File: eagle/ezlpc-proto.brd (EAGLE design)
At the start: 38.1 x 22.9 mm, 61 parts, among them J1 MICRO USB, Q1 12Mhz, T1 MMBT3906, U1 PRTR5V0U2X, U2 MIC5225-3.3v, U3 LPC11U35FHI33/501

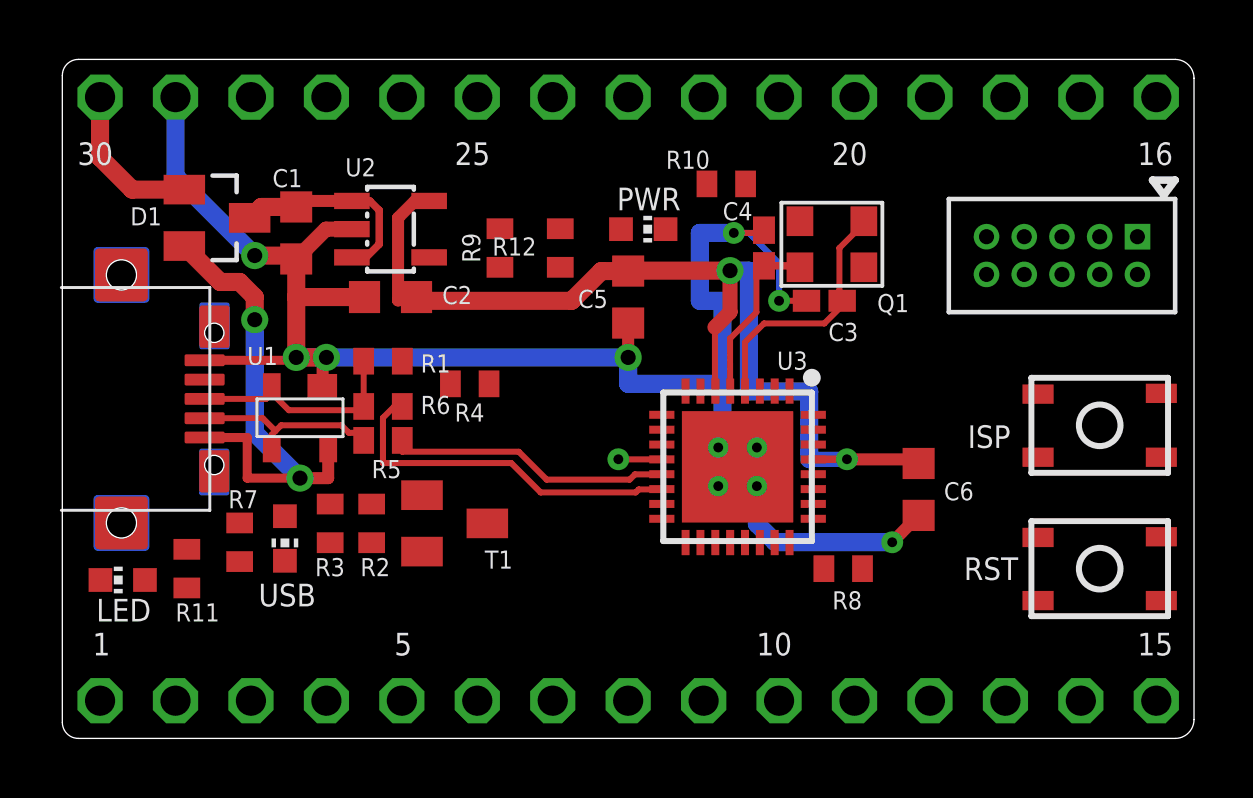
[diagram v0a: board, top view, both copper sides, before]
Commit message: Reduced board height by 0.1" to better fit solderless breadboards.
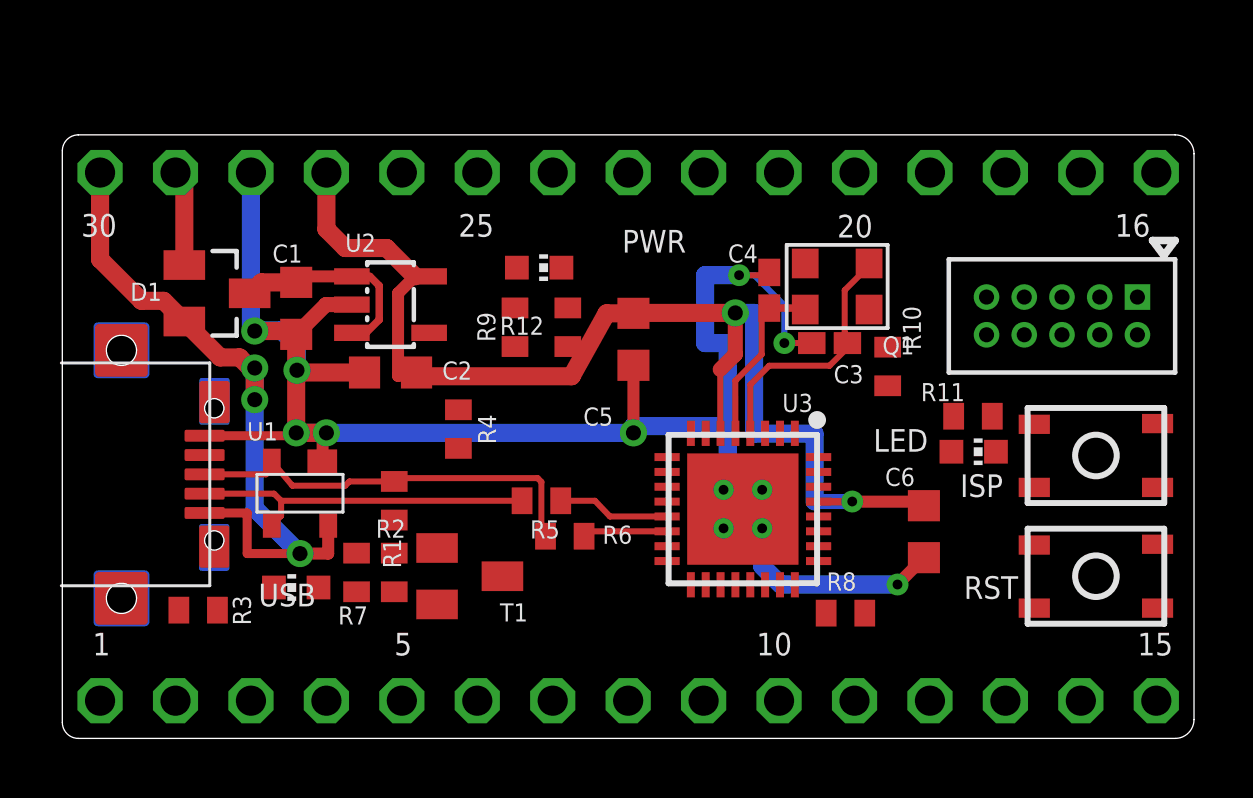
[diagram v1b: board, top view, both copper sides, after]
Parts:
- moved LED2 29.0 mm to (30.7, 9.65), turned to 270 degrees
- moved R11 27.0 mm to (30.7, 10.8), turned to 180 degrees
- moved R10 8.21 mm to (27.8, 12.5), turned to 90 degrees
- moved R6 7.52 mm to (16.9, 6.81)
- moved R5 5.71 mm to (16.1, 8.00)
- moved R3 5.32 mm to (4.57, 4.32), turned to 0 degrees
- moved R1 4.71 mm to (11.2, 8.00), turned to 270 degrees
- moved R7 4.07 mm to (9.91, 5.59), turned to 90 degrees
- moved LED3 3.74 mm to (16.1, 15.8)
- moved R9 2.71 mm to (15.2, 13.8)
- moved R12 2.68 mm to (17.0, 13.8)
- moved C1 2.54 mm to (7.87, 14.5)
- moved C2 2.54 mm to (11.0, 12.3)
- moved D1 2.54 mm to (5.21, 15.0)
- moved J1 2.54 mm to (-0.64, 8.89)
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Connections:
- net AUX-VIN: now also TP29.1; no longer TP30.1
- net GND: now also TP28.1; no longer TP29.1
- net PIO0_10-SWDCLK: now also TP24.1; no longer TP25.1
- net PIO0_21: now also TP1.1; no longer TP2.1
- net PIO0_3-VBUS: now also TP25.1; no longer TP26.1
- net PIO0_5: now also TP26.1; no longer TP28.1
- net PIO0_6-CONNECT: now also TP2.1; no longer TP3.1
- net PIO0_7-LED: now also TP3.1; no longer TP1.1
- net USB-5V: now also TP30.1; no longer TP24.1
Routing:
- net USB_DP: track 12.6 -> 2.86 mm
- net USB-5V: track 16.3 -> 24.0 mm, vias 2 -> 3
- net +3V3: track 34.0 -> 40.6 mm
- net N$8: track 7.62 -> 14.1 mm
- net USB_DM: track 9.59 -> 3.81 mm
- net N$9: track 6.50 -> 11.9 mm
- net GND: track 64.8 -> 66.9 mm, vias 7 -> 8
- net AUX-VIN: track 5.32 -> 3.24 mm
- net PIO0_21: track 1.46 -> 0.00 mm, vias 1 -> 0
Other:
- board size 38.1 x 22.9 mm -> 38.1 x 20.3 mm

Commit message: Ready for final auto routing.
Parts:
- moved R5 0.97 mm to (15.2, 8.00)
- moved C5 0.89 mm to (19.2, 12.5)
- moved R9 0.80 mm to (14.5, 14.0)
- moved R12 0.78 mm to (16.3, 14.0)
- moved LED3 0.74 mm to (15.3, 15.9)
- moved R6 0.71 mm to (16.2, 6.83)
- moved R2 0.38 mm to (11.6, 5.61)
- moved T1 0.31 mm to (14.0, 5.38)
- moved R7 0.20 mm to (10.1, 5.59)
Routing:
- net GND: track 66.9 -> 65.8 mm
- net N$9: track 11.9 -> 11.0 mm
- net USB_DM: track 3.81 -> 4.78 mm
- net USB-5V: track 24.0 -> 24.9 mm, vias 3 -> 4
- net USB_DP: track 2.86 -> 3.55 mm
- net N$8: track 14.1 -> 13.4 mm

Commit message: Ready for final auto routing.
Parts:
- TP1: device ezlpc-proto:1X01 -> ezlpc-proto:1X01-SQUARE
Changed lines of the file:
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@@
 <setting verticaltext="up"/>
 </settings>
-<grid distance="1" unitdist="mil" unit="mil" style="lines" multiple="1" display="yes" altdistance="1" altunitdist="mil" altunit="mil"/>
+<grid distance="50" unitdist="mil" unit="mil" style="lines" multiple="1" display="yes" altdistance="1" altunitdist="mil" altunit="mil"/>
 <layers>
 <layer number="1" name="Top" color="4" fill="1" visible="yes" active="yes"/>
@@
 <param name="mtCopper" value="0.035mm 0.035mm 0.035mm 0.035mm 0.035mm 0.035mm 0.035mm 0.035mm 0.035mm 0.035mm 0.035mm 0.035mm 0.035mm 0.035mm 0.035mm 0.035mm"/>
 <param name="mtIsolate" value="1.5mm 0.15mm 0.2mm 0.15mm 0.2mm 0.15mm 0.2mm 0.15mm 0.2mm 0.15mm 0.2mm 0.15mm 0.2mm 0.15mm 0.2mm"/>
-<param name="mdWireWire" value="6mil"/>
-<param name="mdWirePad" value="6mil"/>
-<param name="mdWireVia" value="6mil"/>
+<param name="mdWireWire" value="7mil"/>
+<param name="mdWirePad" value="7mil"/>
+<param name="mdWireVia" value="7mil"/>
 <param name="mdPadPad" value="8mil"/>
-<param name="mdPadVia" value="6mil"/>
+<param name="mdPadVia" value="8mil"/>
 <param name="mdViaVia" value="8mil"/>
 <param name="mdSmdPad" value="0mil"/>
@@
 <attribute name="VALUE" x="22.86" y="15.875" size="1.27" layer="27"/>
 </element>
-<element name="TP1" library="ezlpc-proto" package="1X01" value="" x="1.27" y="1.27" smashed="yes" rot="R90">
+<element name="TP1" library="ezlpc-proto" package="1X01-SQUARE" value="" x="1.27" y="1.27" smashed="yes" rot="R90">
 <attribute name="NAME" x="0.9398" y="-1.143" size="0.8128" layer="48" font="vector" ratio="10" rot="R270"/>
 <attribute name="VALUE" x="4.445" y="0" size="1.27" layer="27" rot="R90"/>
@@
 <contactref element="U3" pad="G2"/>
 <contactref element="U3" pad="G3"/>
-<wire x1="7.874" y1="10.287" x2="8.763" y2="10.287" width="0.6096" layer="1"/>
+<wire x1="7.874" y1="10.287" x2="8.763" y2="10.287" width="0.8128" layer="1"/>
 <wire x1="8.763" y1="10.287" x2="8.763" y2="9.33" width="0.4064" layer="1"/>
 <wire x1="8.763" y1="9.33" x2="8.751" y2="9.33" width="0.2032" layer="1"/>
@@
 <wire x1="23.5608" y1="8.3716" x2="23.5458" y2="8.3566" width="0.3048" layer="16"/>
 <wire x1="23.5458" y1="8.3566" x2="23.5458" y2="7.0866" width="0.6096" layer="16"/>
-<wire x1="8.89" y1="10.287" x2="7.874" y2="10.287" width="0.6096" layer="16"/>
+<wire x1="8.89" y1="10.287" x2="7.874" y2="10.287" width="0.8128" layer="16"/>
 <via x="19.2278" y="10.287" extent="1-16" drill="0.508"/>
 <via x="28.1178" y="5.1816" extent="1-16" drill="0.3302"/>
@@
 <wire x1="21.6408" y1="15.5956" x2="21.6408" y2="13.3096" width="0.6096" layer="16"/>
 <wire x1="21.6408" y1="13.3096" x2="22.4028" y2="13.3096" width="0.6096" layer="16"/>
-<wire x1="8.89" y1="10.287" x2="19.2278" y2="10.287" width="0.6096" layer="16"/>
+<wire x1="8.89" y1="10.287" x2="19.2278" y2="10.287" width="0.8128" layer="16"/>
 <wire x1="28.1178" y1="5.1816" x2="24.1808" y2="5.1816" width="0.6096" layer="16"/>
 <wire x1="24.1808" y1="5.1816" x2="23.5608" y2="5.8016" width="0.6096" layer="16"/>
@@
 <wire x1="23.2918" y1="15.5956" x2="22.7838" y2="15.5956" width="0.2032" layer="16"/>
 <wire x1="7.874" y1="13.603" x2="7.874" y2="12.319" width="0.6096" layer="1"/>
-<wire x1="7.874" y1="12.319" x2="7.874" y2="10.287" width="0.6096" layer="1"/>
+<wire x1="7.874" y1="12.319" x2="7.874" y2="10.287" width="0.8128" layer="1"/>
 <wire x1="10.174" y1="12.319" x2="7.874" y2="12.319" width="0.6096" layer="1"/>
 <wire x1="7.874" y1="13.603" x2="7.761" y2="13.716" width="0.6096" layer="1"/>
@@
 <wire x1="7.874" y1="10.287" x2="7.777" y2="10.19" width="0.3048" layer="1"/>
 <wire x1="7.777" y1="10.19" x2="4.79" y2="10.19" width="0.3048" layer="1"/>
-<wire x1="6.35" y1="19.05" x2="6.35" y2="13.843" width="0.6096" layer="16"/>
+<wire x1="6.35" y1="19.05" x2="6.35" y2="13.843" width="0.8128" layer="16"/>
 <wire x1="6.35" y1="13.843" x2="6.4516" y2="13.7414" width="0.6096" layer="16"/>
 <via x="7.8994" y="12.3952" extent="1-16" drill="0.508"/>
@@
 <wire x1="7.7978" y1="12.3952" x2="7.8994" y2="12.3952" width="0.6096" layer="16"/>
 <wire x1="7.8994" y1="12.3952" x2="7.9248" y2="12.3952" width="0.6096" layer="16"/>
-<wire x1="6.4516" y1="13.7414" x2="7.366" y2="13.7414" width="0.6096" layer="16"/>
-<wire x1="7.366" y1="13.7414" x2="7.8994" y2="13.208" width="0.6096" layer="16"/>
+<wire x1="6.4516" y1="13.7414" x2="7.366" y2="13.7414" width="0.8128" layer="16"/>
+<wire x1="7.366" y1="13.7414" x2="7.8994" y2="13.208" width="0.8128" layer="16"/>
 <wire x1="7.8994" y1="13.208" x2="7.8994" y2="12.3952" width="0.6096" layer="16"/>
 <wire x1="33.655" y1="14.859" x2="34.925" y2="14.859" width="0" layer="19" extent="1-1"/>
@@
 <wire x1="36.873" y1="8.45" x2="31.4332" y2="9.652" width="0" layer="19" extent="1-1"/>
 <wire x1="36.873" y1="4.386" x2="36.873" y2="8.45" width="0" layer="19" extent="1-1"/>
-<wire x1="19.2278" y1="10.3124" x2="22.4028" y2="10.3124" width="0.6096" layer="16"/>
+<wire x1="19.2278" y1="10.3124" x2="22.4028" y2="10.3124" width="0.8128" layer="16"/>
 </signal>
 <signal name="N$1">

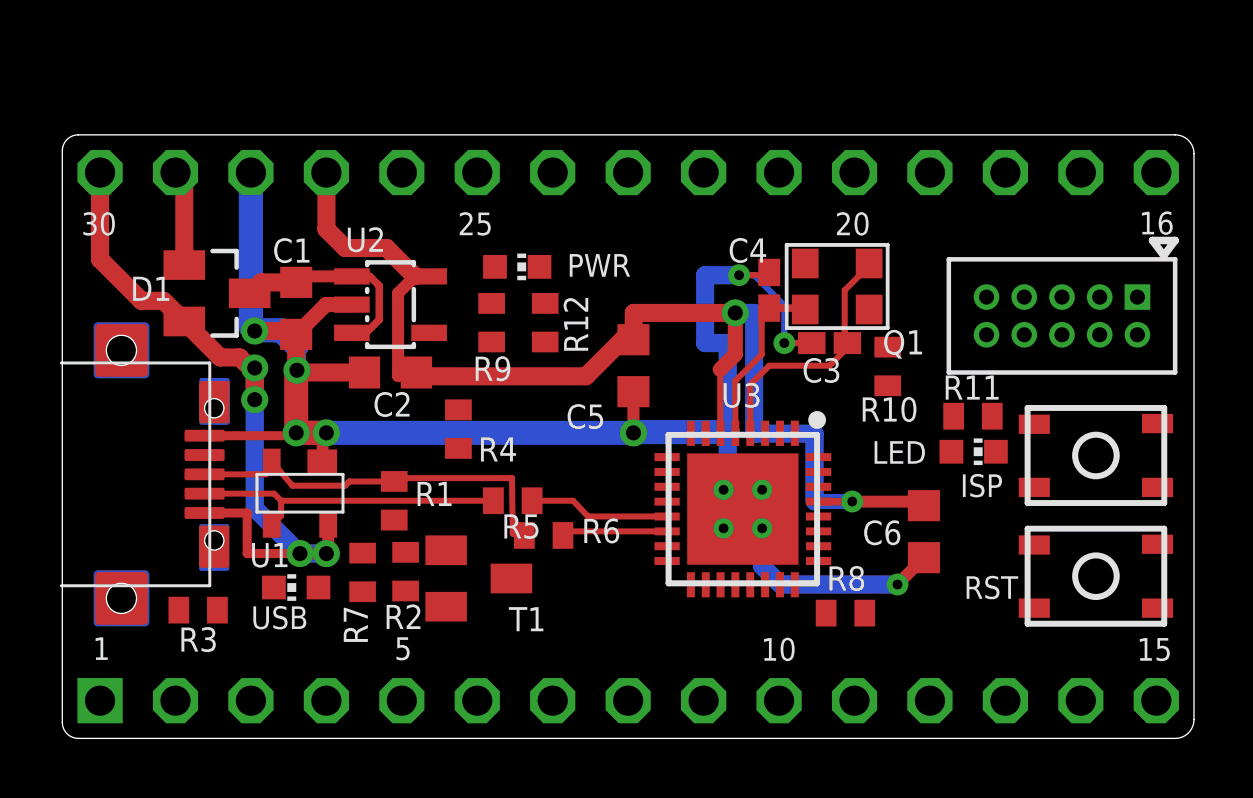
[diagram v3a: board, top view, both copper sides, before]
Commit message: Added BOM.
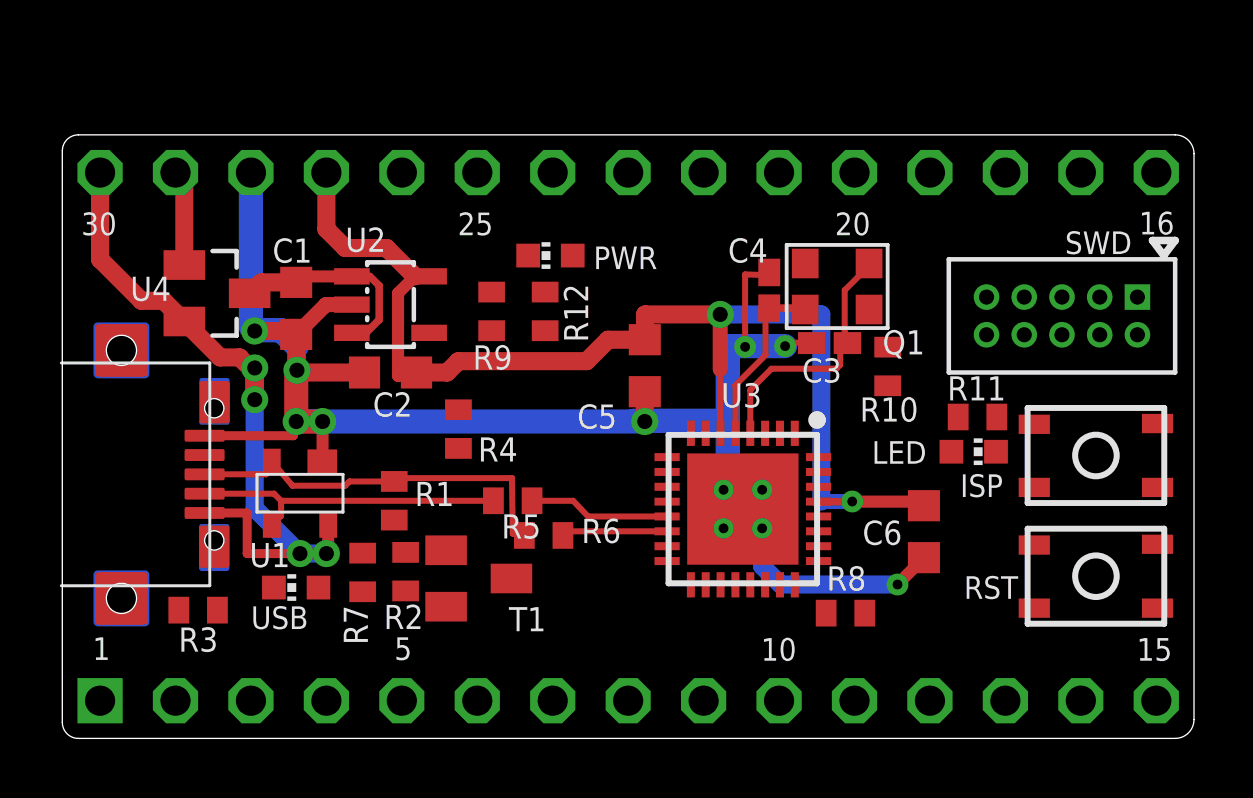
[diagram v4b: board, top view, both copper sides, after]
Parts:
- LED1: value (none) -> Green
- LED2: value (none) -> Red
- LED3: value (none) -> Blue
- R11, R12, R3, R4, R7: value 2K -> 1K5
- R2, R8, R9: value 24K -> 10K
- moved LED3 1.18 mm to (16.4, 16.3), turned to 90 degrees
- moved C5 0.38 mm to (19.6, 12.5)
- moved R12 0.38 mm to (16.3, 14.4)
- moved R9 0.38 mm to (14.5, 14.4)
- moved R11 0.15 mm to (30.8, 10.8)
- renumbered D1 to U4
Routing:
- net USB-5V: track 24.9 -> 26.0 mm
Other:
- board text added: "SWD"

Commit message: Turned the SWD connector
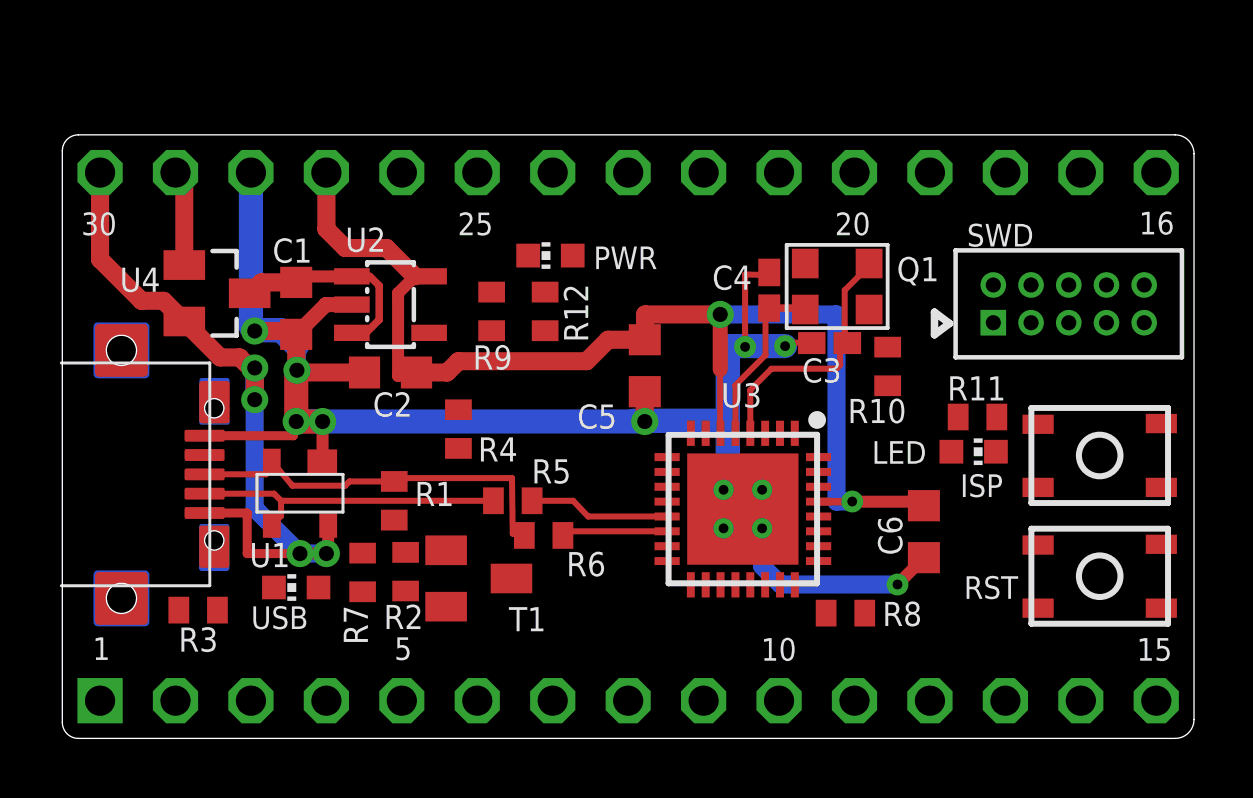
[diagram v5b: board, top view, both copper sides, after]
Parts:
- moved J2 2.32 mm to (33.9, 14.6), turned to 0 degrees
- moved S1 0.13 mm to (34.9, 5.46)
- moved S2 0.13 mm to (34.9, 9.53)

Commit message: Minor net rename.
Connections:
- net PIO0_9-SWD6 renamed PIO0_9-SWDO
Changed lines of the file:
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@@
 <wire x1="4.107" y1="18.753" x2="4.107" y2="15.936" width="0.6096" layer="1"/>
 </signal>
-<signal name="PIO0_9-SWD6">
+<signal name="PIO0_9-SWDO">
 <contactref element="J2" pad="6"/>
 </signal>
